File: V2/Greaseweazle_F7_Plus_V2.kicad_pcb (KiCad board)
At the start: 2 copper layers, 80 x 50 mm, 83 parts, among them J1 Wurth 694106301002, J10 PIN1X2, J11 PIN1X2, J12 IDC Box Header, J2 USB_B, J3 Molex 105017-1001, J4 TE EI 171826-4, J5 PIN1X3, J6 PIN1X2, J7 PIN1X5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

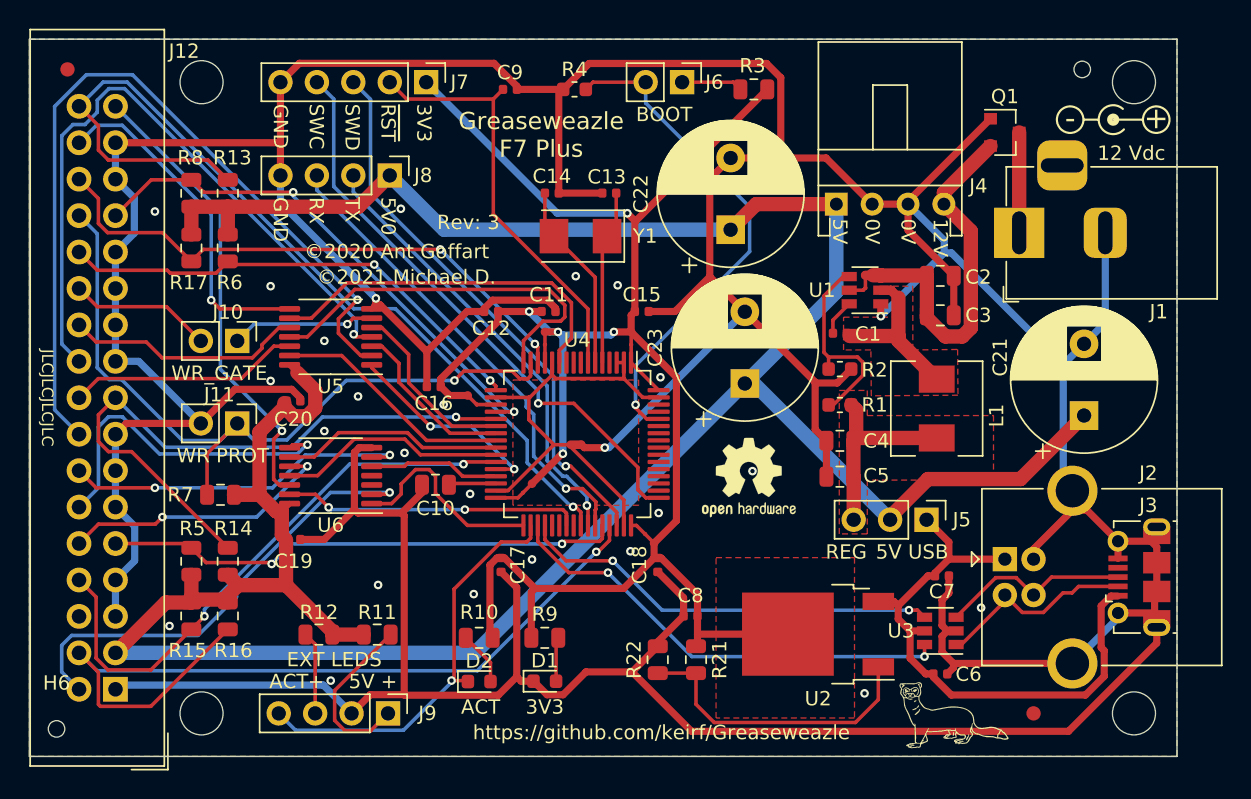
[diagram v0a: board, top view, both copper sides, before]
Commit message: added user pin connector removed C23
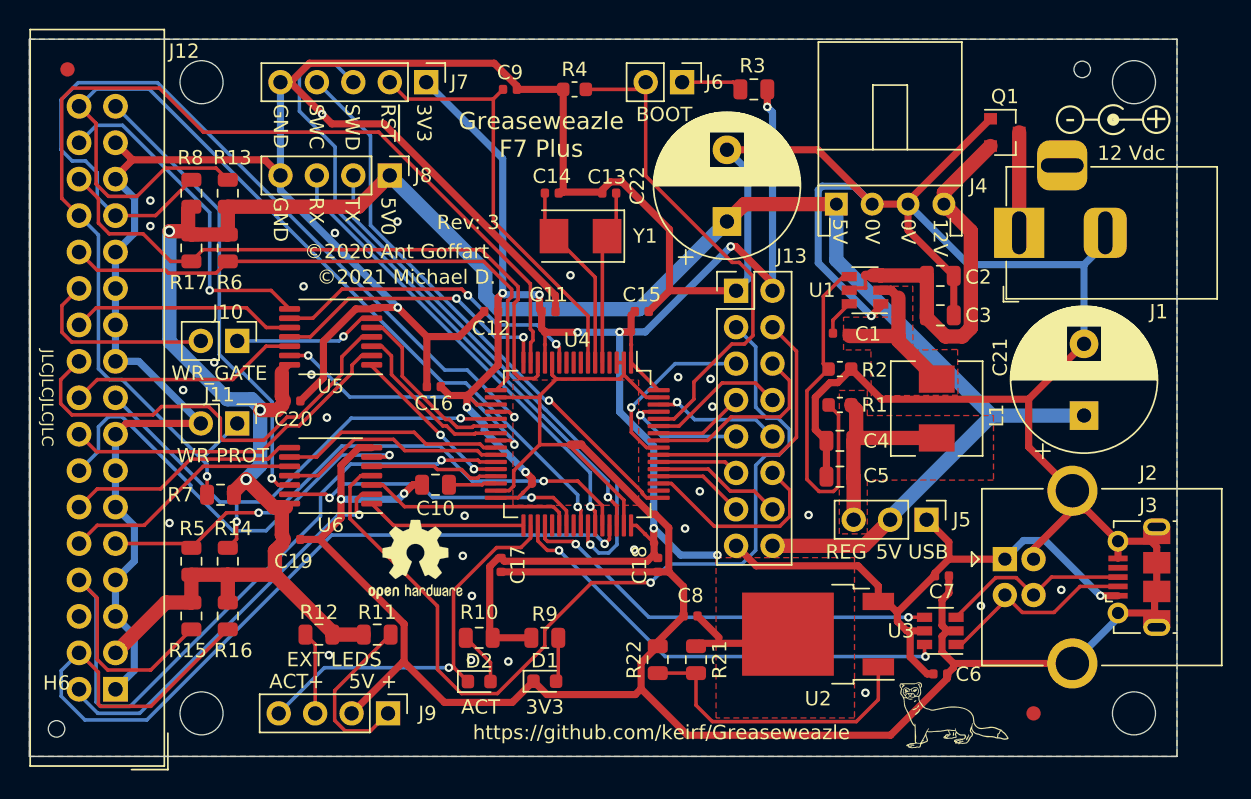
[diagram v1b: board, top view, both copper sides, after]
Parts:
- removed C23: 1000uF, Capacitor_THT:CP_Radial_D10.0mm_P5.00mm
- added J13: Conn_02x05_Odd_Even, Connector_PinHeader_2.54mm:PinHeader_2x08_P2.54mm_Vertical, F.Cu at (199.3, 117.5)
- moved LOGO1 23.9 mm to (176.9, 136.3)
- moved C22 0.63 mm to (198.6, 112.7)
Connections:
- U4 pad 38: (no net) -> /~USER_PIN1_OUT~
- U4 pad 51: (no net) -> /~USER_PIN10~
- U4 pad 52: (no net) -> /~USER_PIN11~
- U4 pad 53: (no net) -> /~USER_PIN12~
- U4 pad 54: (no net) -> /~USER_PIN9~
- U4 pad 55: (no net) -> /~USER_PIN2~
- U4 pad 56: (no net) -> /~USER_PIN3~
- U4 pad 57: (no net) -> /~USER_PIN4~
- U4 pad 58: (no net) -> /~USER_PIN5~
- U4 pad 59: (no net) -> /~USER_PIN6~
- U4 pad 61: (no net) -> /~USER_PIN7~
- U4 pad 62: (no net) -> /~USER_PIN8~
- U6 pad 3: (no net) -> /~USER_PIN1_OUT~
- U6 pad 4: (no net) -> /~USER_PIN1_OUT_5V~
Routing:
- net /~USER_PIN1_OUT_5V~: track 0.00 -> 63.9 mm, vias 0 -> 1
- net /~M1_5V~: track 57.9 -> 24.0 mm, vias 1 -> 0
- net +5V: track 196.9 -> 165.2 mm, vias 0 -> 3
- net /~WR_PROT~: track 53.5 -> 80.1 mm
- net /~MTYPE_ID0~: track 37.0 -> 59.7 mm, vias 2 -> 1
- net /~INDEX~: track 40.4 -> 59.1 mm, vias 2 -> 1
- net /~USER_PIN2~: track 0.00 -> 18.5 mm
- net /~STEP_5V~: track 47.7 -> 31.2 mm, vias 1 -> 0
- net /~USER_PIN1_OUT~: track 0.00 -> 14.8 mm
- net /~USER_PIN10~: track 0.00 -> 14.2 mm
- net /~USER_PIN4~: track 0.00 -> 13.6 mm
- net /~USER_PIN3~: track 0.00 -> 12.7 mm, vias 0 -> 1
- net /FB: track 14.2 -> 24.6 mm
- net /~USER_PIN6~: track 0.00 -> 9.68 mm
- net /~USER_PIN12~: track 0.00 -> 9.10 mm
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
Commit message: moved user pin conn and voltage reg to make more space for the casing of the user pin conn
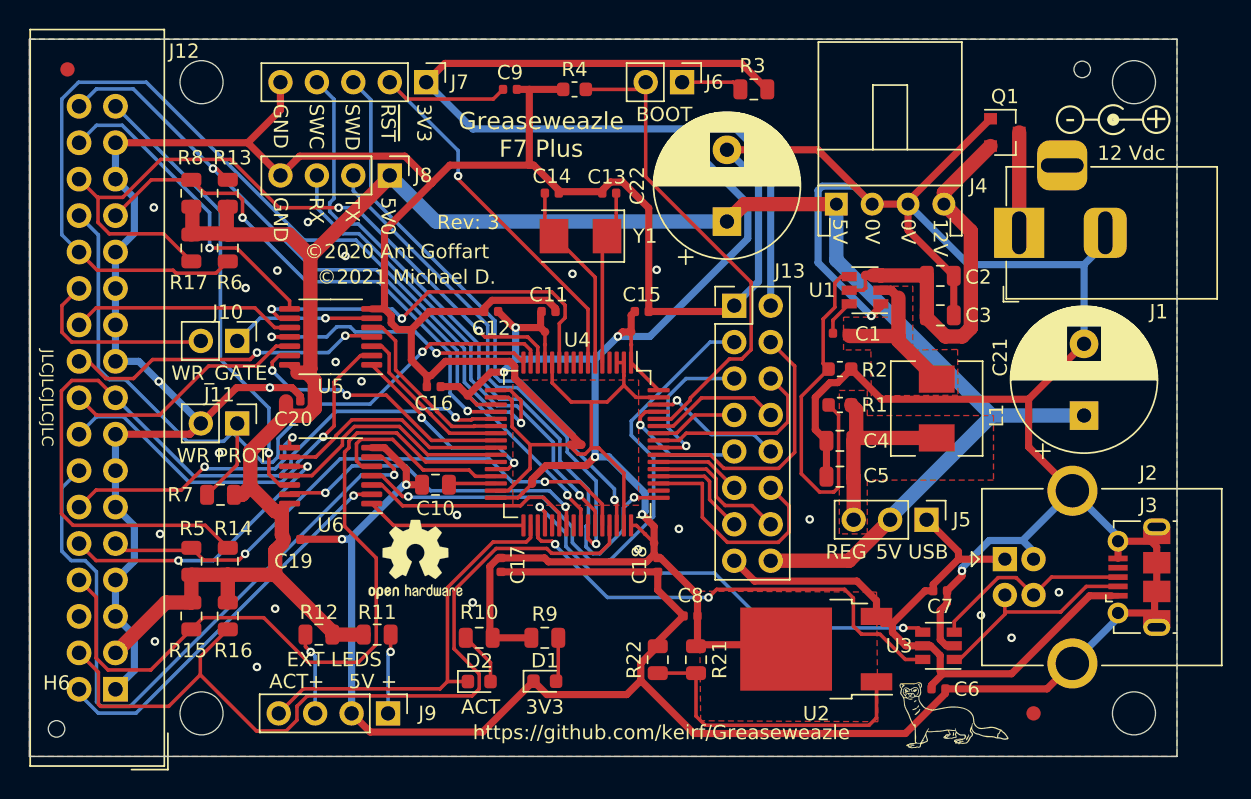
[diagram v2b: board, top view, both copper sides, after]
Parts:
- moved C7 1.05 mm to (213.5, 138.5)
- moved C6 1.05 mm to (213.4, 145.3)
- moved J13 1.05 mm to (199.1, 118.6)
- moved U2 1.05 mm to (204.9, 142.5)
- moved U3 1.05 mm to (213.4, 142.3)
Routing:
- net +3V3: track 124.8 -> 161.5 mm, vias 10 -> 5
- net /~TRK_00~: track 39.4 -> 69.8 mm, vias 0 -> 1
- net /~WR_PROT~: track 80.1 -> 56.4 mm
- net /~USER_PIN1_OUT_5V~: track 63.9 -> 40.8 mm
- net /~MTYPE_ID0~: track 59.7 -> 36.6 mm, vias 1 -> 2
- net /~MTYPE_ID1~: track 35.4 -> 57.1 mm, vias 2 -> 1
- net /~DS0_5V~: track 31.1 -> 48.1 mm
- net /~DISK_CHANGE~: track 65.8 -> 51.7 mm, vias 1 -> 2
- net GND: track 447.5 -> 434.7 mm, vias 32 -> 28
- net /SWCLK: track 39.5 -> 49.8 mm
- net +5V: track 165.2 -> 155.0 mm, vias 3 -> 0
- net /~STEP_5V~: track 31.2 -> 22.2 mm, vias 0 -> 2
- net Net-(J9-Pad1): track 12.1 -> 5.57 mm, vias 0 -> 1
- net /USB_VBUS: track 43.1 -> 48.9 mm, vias 1 -> 0
- net /SWDIO: track 45.1 -> 39.3 mm
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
